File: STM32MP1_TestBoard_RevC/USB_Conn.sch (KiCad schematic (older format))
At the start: 4 parts, among them J13 USB_B_Micro, J8 USB_B_Micro

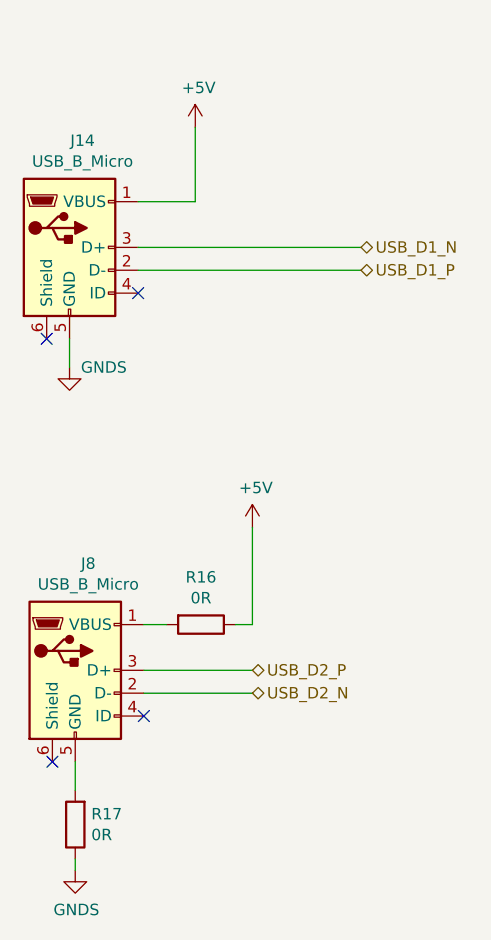
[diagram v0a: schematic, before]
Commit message: HW changes
- Changed buck converter(TPS42402) to LDO (AZ1117)
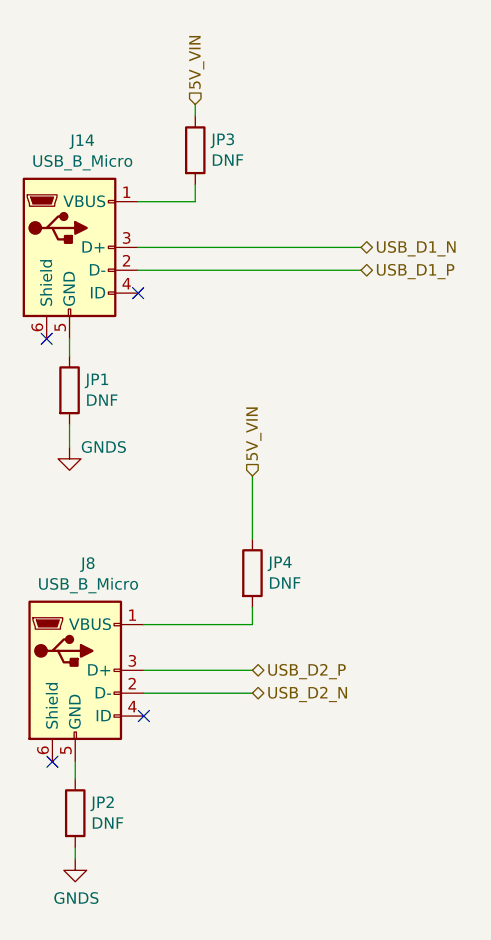
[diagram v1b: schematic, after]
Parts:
- removed R16, R17: 0R, Resistor_SMD:R_0402_1005Metric_Pad0.72x0.64mm_HandSolder, symbol Device:R
- added JP1, JP2, JP3, JP4: DNF, Resistor_SMD:R_0402_1005Metric_Pad0.72x0.64mm_HandSolder, symbol Device:R
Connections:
- net GNDS: now also JP1.2, JP2.2; no longer J13.5 (GND)
- net at J8.1 (VBUS): now also JP4.2
- net at J8.5 (GND): now also JP2.1
- net +5V: no longer names the net of J13.1 (VBUS)
- net +5V: now also JP3.2
- new net: J13.5 (GND), JP1.1
- new net 5V_VIN: JP3.1, JP4.1
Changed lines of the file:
@@
 $Descr A4 11693 8268
 encoding utf-8
-Sheet 9 9
+Sheet 8 9
 Title ""
 Date "2021-06-13"
@@
 L power:GNDS #PWR0128
 U 1 1 611068FF
-P 4625 3725
+P 4625 4075
 AR Path="/610FE7C3/611068FF" Ref="#PWR0128"  Part="1"
 AR Path="/6097C138/609989A6/611068FF" Ref="#PWR047"  Part="1"
-F 0 "#PWR047" H 4625 3475 50  0001 C CNN
-F 1 "GNDS" H 4775 3725 50  0000 C CNN
-F 2 "" H 4625 3725 50  0001 C CNN
-F 3 "" H 4625 3725 50  0001 C CNN
-	1    4625 3725
+F 0 "#PWR047" H 4625 3825 50  0001 C CNN
+F 1 "GNDS" H 4775 4075 50  0000 C CNN
+F 2 "" H 4625 4075 50  0001 C CNN
+F 3 "" H 4625 4075 50  0001 C CNN
+	1    4625 4075
 	1    0    0    -1
 $EndComp
@@
 	4925 3000 5175 3000
 Wire Wire Line
-	5175 3000 5175 2675
-$Comp
-L power:+5V #PWR0129
-U 1 1 6110690A
-P 5175 2675
-AR Path="/610FE7C3/6110690A" Ref="#PWR0129"  Part="1"
-AR Path="/6097C138/609989A6/6110690A" Ref="#PWR050"  Part="1"
-F 0 "#PWR050" H 5175 2525 50  0001 C CNN
-F 1 "+5V" H 5190 2848 50  0000 C CNN
-F 2 "" H 5175 2675 50  0001 C CNN
-F 3 "" H 5175 2675 50  0001 C CNN
-	1    5175 2675
-	1    0    0    -1
-$EndComp
+	5175 3000 5175 2925
 Wire Wire Line
-	5425 4850 5425 4425
-$Comp
-L power:+5V #PWR0131
-U 1 1 6110691F
-P 5425 4425
-AR Path="/610FE7C3/6110691F" Ref="#PWR0131"  Part="1"
-AR Path="/6097C138/609989A6/6110691F" Ref="#PWR051"  Part="1"
-F 0 "#PWR051" H 5425 4275 50  0001 C CNN
-F 1 "+5V" H 5440 4598 50  0000 C CNN
-F 2 "" H 5425 4425 50  0001 C CNN
-F 3 "" H 5425 4425 50  0001 C CNN
-	1    5425 4425
-	1    0    0    -1
-$EndComp
+	5425 4850 5425 4775
 Wire Wire Line
 	4950 5050 5425 5050
@@
 L power:GNDS #PWR0132
 U 1 1 61106928
-P 4650 5925
+P 4650 5875
 AR Path="/610FE7C3/61106928" Ref="#PWR0132"  Part="1"
 AR Path="/6097C138/609989A6/61106928" Ref="#PWR048"  Part="1"
-F 0 "#PWR048" H 4650 5675 50  0001 C CNN
-F 1 "GNDS" H 4655 5752 50  0000 C CNN
-F 2 "" H 4650 5925 50  0001 C CNN
-F 3 "" H 4650 5925 50  0001 C CNN
-	1    4650 5925
+F 0 "#PWR048" H 4650 5625 50  0001 C CNN
+F 1 "GNDS" H 4655 5702 50  0000 C CNN
+F 2 "" H 4650 5875 50  0001 C CNN
+F 3 "" H 4650 5875 50  0001 C CNN
+	1    4650 5875
 	1    0    0    -1
 $EndComp
@@
 NoConn ~ 4525 3600
 Wire Wire Line
-	4625 3600 4625 3725
+	4625 3600 4625 3675
 $Comp
 L Connector:USB_B_Micro J?
@@
 NoConn ~ 4950 5250
 Wire Wire Line
-	4950 4850 5050 4850
+	4650 5450 4650 5525
 Wire Wire Line
-	4650 5450 4650 5575
+	4650 5825 4650 5875
+Wire Wire Line
+	4625 4075 4625 3975
+Wire Wire Line
+	4950 4850 5425 4850
+Wire Wire Line
+	5175 2625 5175 2575
 $Comp
-L Device:R R16
-U 1 1 5FC7250A
-P 5200 4850
-F 0 "R16" V 4993 4850 50  0000 C CNN
-F 1 "0R" V 5084 4850 50  0000 C CNN
-F 2 "Resistor_SMD:R_0402_1005Metric_Pad0.72x0.64mm_HandSolder" V 5130 4850 50  0001 C CNN
-F 3 "~" H 5200 4850 50  0001 C CNN
-F 4 "~" H 5200 4850 50  0001 C CNN "Mfr"
-F 5 "~" H 5200 4850 50  0001 C CNN "PartNo"
-F 6 "C25087" H 5200 4850 50  0001 C CNN "LCSC"
-F 7 "~" H 5200 4850 50  0001 C CNN "Comment"
-F 8 "~" H 5200 4850 50  0001 C CNN "Mouser"
-	1    5200 4850
-	0    1    1    0
+L Device:R JP3
+U 1 1 612F340A
+P 5175 2775
+F 0 "JP3" H 5245 2821 50  0000 L CNN
+F 1 "DNF" H 5245 2730 50  0000 L CNN
+F 2 "Resistor_SMD:R_0402_1005Metric_Pad0.72x0.64mm_HandSolder" V 5105 2775 50  0001 C CNN
+F 3 "~" H 5175 2775 50  0001 C CNN
+	1    5175 2775
+	1    0    0    -1
 $EndComp
+$Comp
+L Device:R JP1
+U 1 1 612F51C4
+P 4625 3825
+F 0 "JP1" H 4695 3871 50  0000 L CNN
+F 1 "DNF" H 4695 3780 50  0000 L CNN
+F 2 "Resistor_SMD:R_0402_1005Metric_Pad0.72x0.64mm_HandSolder" V 4555 3825 50  0001 C CNN
+F 3 "~" H 4625 3825 50  0001 C CNN
+	1    4625 3825
+	1    0    0    -1
+$EndComp
+$Comp
+L Device:R JP4
+U 1 1 612F62A5
+P 5425 4625
+F 0 "JP4" H 5495 4671 50  0000 L CNN
+F 1 "DNF" H 5495 4580 50  0000 L CNN
+F 2 "Resistor_SMD:R_0402_1005Metric_Pad0.72x0.64mm_HandSolder" V 5355 4625 50  0001 C CNN
+F 3 "~" H 5425 4625 50  0001 C CNN
+	1    5425 4625
+	1    0    0    -1
+$EndComp
+$Comp
+L Device:R JP2
+U 1 1 612F7543
+P 4650 5675
+F 0 "JP2" H 4720 5721 50  0000 L CNN
+F 1 "DNF" H 4720 5630 50  0000 L CNN
+F 2 "Resistor_SMD:R_0402_1005Metric_Pad0.72x0.64mm_HandSolder" V 4580 5675 50  0001 C CNN
+F 3 "~" H 4650 5675 50  0001 C CNN
+	1    4650 5675
+	1    0    0    -1
+$EndComp
+Text HLabel 5175 2575 1    50   Input ~ 0
+5V_VIN
+Text HLabel 5425 4200 1    50   Input ~ 0
+5V_VIN
 Wire Wire Line
-	5350 4850 5425 4850
-$Comp
-L Device:R R17
-U 1 1 5FC752AF
-P 4650 5725
-F 0 "R17" H 4580 5679 50  0000 R CNN
-F 1 "0R" H 4580 5770 50  0000 R CNN
-F 2 "Resistor_SMD:R_0402_1005Metric_Pad0.72x0.64mm_HandSolder" V 4580 5725 50  0001 C CNN
-F 3 "~" H 4650 5725 50  0001 C CNN
-F 4 "~" H 4650 5725 50  0001 C CNN "Mfr"
-F 5 "~" H 4650 5725 50  0001 C CNN "PartNo"
-F 6 "C25087" H 4650 5725 50  0001 C CNN "LCSC"
-F 7 "~" H 4650 5725 50  0001 C CNN "Comment"
-F 8 "~" H 4650 5725 50  0001 C CNN "Mouser"
-	1    4650 5725
-	-1   0    0    1
-$EndComp
-Wire Wire Line
-	4650 5875 4650 5925
+	5425 4200 5425 4475
 $EndSCHEMATC
